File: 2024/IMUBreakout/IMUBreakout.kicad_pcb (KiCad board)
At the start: 2 copper layers, 8 parts, among them J1 SM06B-GHS-TB_LF__SN_, SW1 SW_Push, U1 BNO085

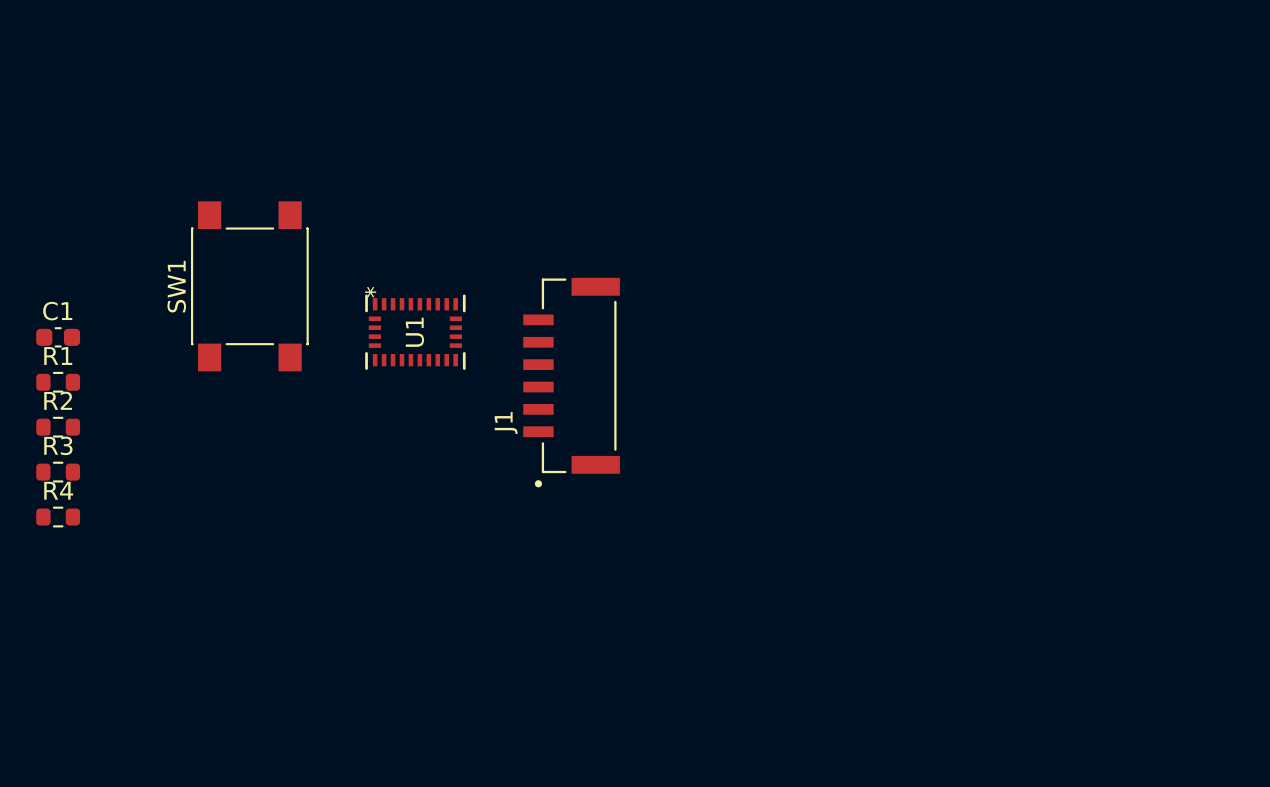
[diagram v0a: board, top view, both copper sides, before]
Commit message: Connected all pins on IMU breakout PBC editor
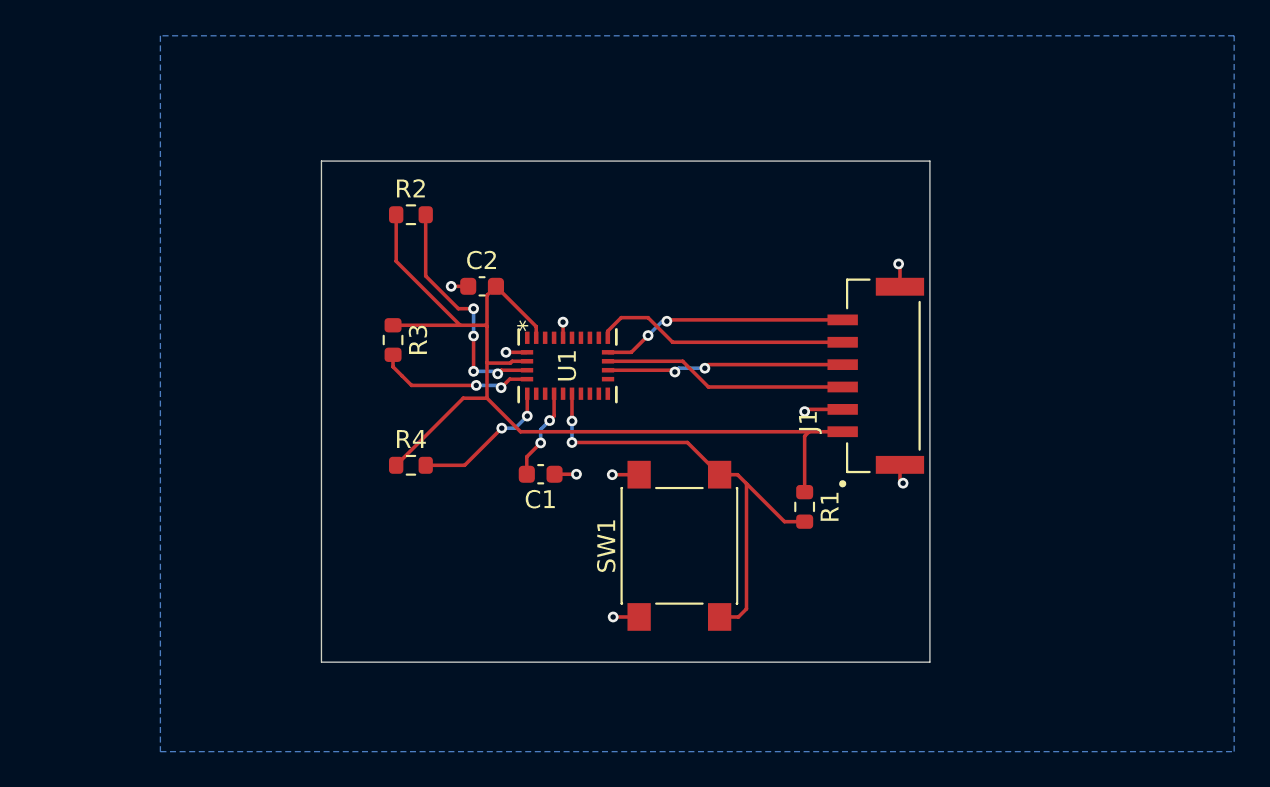
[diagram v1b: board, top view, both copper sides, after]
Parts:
- added C2: 1u, Capacitor_SMD:C_0603_1608Metric, F.Cu at (128.0, 64.0)
- moved R1 42.3 mm to (146.0, 76.3), turned to -90 degrees
- moved SW1 28.0 mm to (139.0, 78.5)
- moved C1 28.0 mm to (131.2, 74.5), turned to 180 degrees
- moved R2 23.0 mm to (124.0, 60.0)
- moved R3 20.1 mm to (123.0, 67.0), turned to -90 degrees
- moved R4 19.9 mm to (124.0, 74.0)
- moved J1 17.0 mm to (150.0, 69.0)
- moved U1 8.70 mm to (132.8, 68.4)
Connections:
- U1 pad 3: +3V3 -> +3.3V
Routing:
- net +3.3V: track 0.00 -> 56.3 mm
- net Net-(U1-NRST): track 0.00 -> 26.8 mm, vias 0 -> 2
- net H_SDA/H_MISO: track 0.00 -> 14.4 mm
- net SCK: track 0.00 -> 13.9 mm, vias 0 -> 2
- net H_CSN: track 0.00 -> 13.7 mm
- net Net-(U1-BOOTN): track 0.00 -> 13.5 mm, vias 0 -> 4
- net  SA0/H_MOSI: track 0.00 -> 13.3 mm, vias 0 -> 2
- net GND: track 0.00 -> 11.8 mm, vias 0 -> 9
- net Net-(U1-PS1): track 0.00 -> 8.84 mm, vias 0 -> 2
- net Net-(U1-PS0/WAKE): track 0.00 -> 8.06 mm, vias 0 -> 2
- net Net-(U1-CAP): track 0.00 -> 5.13 mm, vias 0 -> 2
- added copper zone on B.Cu, net GND
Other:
- board outline added: 34 x 28 mm
